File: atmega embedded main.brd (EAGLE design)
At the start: 354.1 x 155.8 mm, 144 parts, among them IC1 ATMEGA328PROUND, K100 SWITCH, K101 SWITCH, K102 SWITCH, K103 SWITCH, K104 SWITCH, K105 SWITCH, K106 SWITCH, K107 SWITCH, K108 SWITCH, K109 SWITCH, K110 SWITCH, K111 SWITCH, K112 SWITCH, K113 SWITCH, K114 SWITCH, K115 SWITCH, K116 SWITCH, K117 SWITCH, K118 SWITCH, K119 SWITCH, K120 SWITCH, K121 SWITCH, K122 SWITCH, K123 SWITCH, K124 SWITCH, K125 SWITCH, K126 SWITCH, K127 SWITCH, K128 SWITCH, K129 SWITCH, K130 SWITCH, K60 SWITCH, K67 SWITCH, K68 SWITCH, K69 SWITCH, K70 SWITCH, K71 SWITCH, K72 SWITCH, K73 SWITCH, K74 SWITCH, K75 SWITCH, K76 SWITCH, K77 SWITCH, K78 SWITCH, K79 SWITCH, K80 SWITCH, K81 SWITCH, K82 SWITCH, K83 SWITCH, K84 SWITCH, K85 SWITCH, K86 SWITCH, K87 SWITCH, K88 SWITCH, K89 SWITCH, K90 SWITCH, K91 SWITCH, K92 SWITCH, K93 SWITCH, K94 SWITCH, K95 SWITCH, K96 SWITCH, K97 SWITCH, K98 SWITCH, K99 SWITCH

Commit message: Flipped switches and rewired everything
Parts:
- moved R7 65.8 mm to (33.2, 114.0), turned to 90 degrees
- moved R6 64.6 mm to (35.6, 114.0), turned to 90 degrees
- moved D129 17.3 mm to (173.4, 4.75), flipped to the bottom, turned to 0 degrees
- moved D100 14.2 mm to (201.9, 80.8), flipped to the bottom
- moved D101 14.2 mm to (220.9, 80.8), flipped to the bottom
- moved D102 14.2 mm to (239.9, 80.8), flipped to the bottom
- moved D106 14.2 mm to (239.9, 61.8), flipped to the bottom
- moved D107 14.2 mm to (220.9, 61.8), flipped to the bottom
- moved D108 14.2 mm to (201.9, 61.8), flipped to the bottom
- moved D109 14.2 mm to (182.9, 61.8), flipped to the bottom
- moved D111 14.2 mm to (201.9, 4.75), flipped to the bottom
- moved D112 14.2 mm to (220.9, 4.75), flipped to the bottom
- moved D113 14.2 mm to (239.9, 4.75), flipped to the bottom
- moved D114 14.2 mm to (258.9, 4.75), flipped to the bottom
- moved D118 14.2 mm to (182.9, 42.8), flipped to the bottom
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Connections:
- new net N$42: D115.C, K104.P$1
- net COL1: now also IC1.11
- net COL10: now also IC1.3, K104.P$2; no longer K104.P$1
- net COL2: now also IC1.12
- net COL3: now also IC1.13
- net COL4: now also IC1.14
- net COL5: now also IC1.25
- net COL6: now also IC1.26, K118.P$2; no longer K118.P$1
- net COL7: now also IC1.27, K111.P$2, K128.P$2; no longer K111.P$1, K128.P$1
- net COL8: now also IC1.28, K105.P$2, K123.P$2; no longer K105.P$1, K123.P$1
- net COL9: now also IC1.2, K117.P$2, K98.P$2; no longer K117.P$1, K98.P$1
- net D+: now also R7.2; no longer IC1.23, R6.1, R6.2
- net D-: now also R6.2; no longer R7.2
- net N$21: now also IC1.6; no longer IC1.24
- net N$27: now also D116.C, K98.P$1; no longer D98.C, K118.P$2
- net N$28: now also D117.C, K105.P$1; no longer D110.C, K111.P$2
- net N$40: now also D110.C, K111.P$1; no longer D117.C, K105.P$2
- net N$41: now also D98.C, K118.P$1; no longer D116.C, K98.P$2
- net N$65: now also D128.C, K117.P$1; no longer D115.C, K104.P$2
- net N$66: now also D127.C, K123.P$1; no longer D128.C, K117.P$2
- net N$67: now also D104.C, K128.P$1; no longer D127.C, K123.P$2
- net N$68: now also IC1.5, R6.1; no longer D104.C, K128.P$2
- net ROW1: now also IC1.23
- net ROW2: now also IC1.19
- net ROW3: now also IC1.18
- net ROW4: now also IC1.17
- net ROW5: now also IC1.16
- net ROW6: now also IC1.15
- net ROW7: now also IC1.24
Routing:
- net COL9: track 109.5 -> 436.6 mm, vias 0 -> 2
- net COL8: track 104.0 -> 408.8 mm, vias 0 -> 2
- net ROW6: track 170.5 -> 462.1 mm, vias 0 -> 2
- net COL7: track 104.0 -> 393.0 mm, vias 0 -> 2
- net ROW3: track 369.7 -> 645.3 mm, vias 0 -> 2
- net ROW5: track 479.1 -> 751.6 mm, vias 0 -> 2
- net ROW4: track 389.8 -> 659.2 mm, vias 0 -> 2
- net ROW2: track 330.0 -> 599.1 mm, vias 0 -> 2
- net COL10: track 110.5 -> 351.7 mm, vias 0 -> 2
- net COL4: track 104.0 -> 329.2 mm, vias 0 -> 1
- net COL3: track 104.0 -> 326.7 mm, vias 0 -> 1
- net COL2: track 116.6 -> 321.6 mm, vias 0 -> 1
- net COL5: track 111.2 -> 303.2 mm, vias 0 -> 1
- net COL6: track 104.4 -> 287.2 mm, vias 0 -> 2
- net ROW7: track 119.7 -> 270.6 mm, vias 0 -> 2
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
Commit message: Compacted stuff around the chip
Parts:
- moved C3 29.0 mm to (106.9, 106.9)
- moved R5 28.2 mm to (78.4, 104.5)
- moved C4 27.1 mm to (102.1, 106.9)
- moved S1 26.6 mm to (83.1, 97.4)
- moved C5 25.2 mm to (97.4, 106.9)
- moved C6 23.5 mm to (92.6, 106.9)
- moved C7 21.9 mm to (87.9, 106.9)
- moved C10 18.6 mm to (37.4, 114.0), turned to 0 degrees
- moved U1 18.1 mm to (73.6, 115.2)
- moved C9 16.4 mm to (37.4, 111.6), turned to 0 degrees
- moved R7 12.2 mm to (44.5, 109.2), flipped to the bottom
- moved Q1 9.67 mm to (30.9, 112.2), turned to 313.5 degrees
- moved IC1 8.56 mm to (35.6, 102.1)
- moved R6 7.60 mm to (41.6, 109.2)
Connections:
- net N$21: now also IC1.4; no longer IC1.6
- net ROW5: now also IC1.15; no longer IC1.16
- net ROW6: now also IC1.16; no longer IC1.15
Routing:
- net GND: track 80.6 -> 148.2 mm, vias 4 -> 3
- net VCC: track 51.2 -> 114.8 mm
- net ROW5: track 751.6 -> 770.8 mm
- net N$15: track 17.7 -> 36.2 mm
- net ROW6: track 462.1 -> 475.9 mm
- net COL10: track 351.7 -> 340.8 mm
- net ROW7: track 270.6 -> 260.1 mm
- net COL4: track 329.2 -> 319.3 mm
- net COL6: track 287.2 -> 277.7 mm
- net COL3: track 326.7 -> 317.6 mm
- net ROW1: track 376.0 -> 383.8 mm
- net COL9: track 436.6 -> 428.9 mm
- net D-: track 39.3 -> 46.8 mm
- net COL8: track 408.8 -> 401.5 mm
- net COL1: track 212.0 -> 204.9 mm
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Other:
- board size 354.1 x 155.8 mm -> 313.5 x 125.9 mm

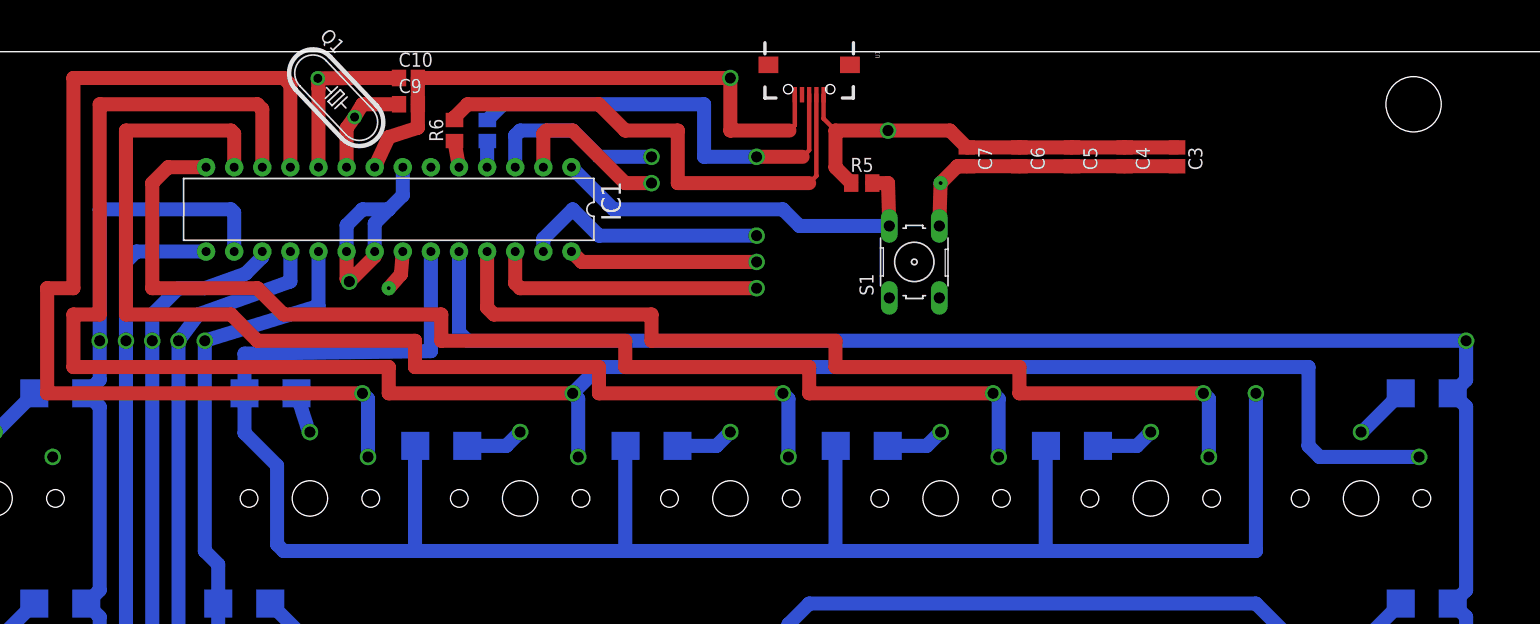
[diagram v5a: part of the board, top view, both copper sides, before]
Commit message: Fixed errors and made adjustments for USB
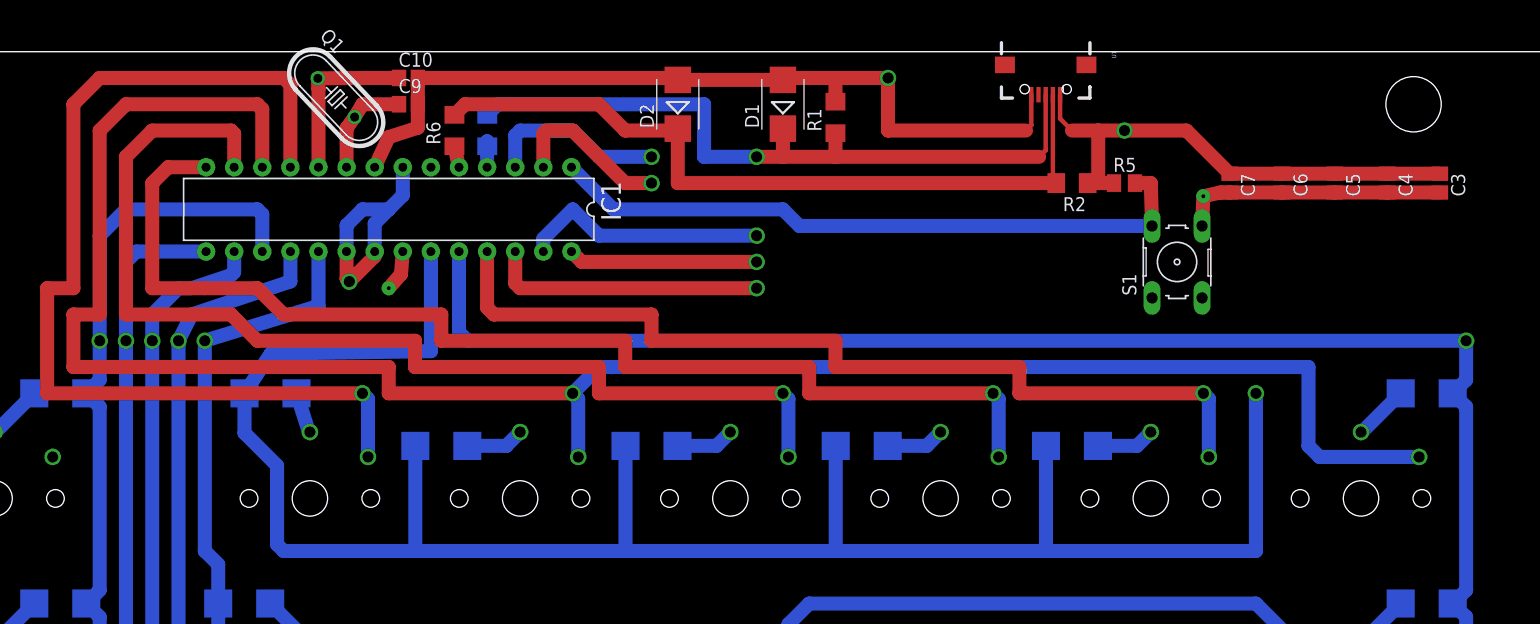
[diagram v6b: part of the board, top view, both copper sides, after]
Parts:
- added D1, D2: 3.6, diode:SMB
- added R1: 1M, eagle-ltspice:R1206
- added R2: 1.5K, eagle-ltspice:R1206
- R6, R7: value 22 -> 68; device adafruit:M0805 -> eagle-ltspice:R1206
- moved C3 23.9 mm to (130.6, 104.5)
- moved C4 23.9 mm to (125.9, 104.5)
- moved C5 23.9 mm to (121.1, 104.5)
- moved C6 23.9 mm to (116.4, 104.5)
- moved C7 23.9 mm to (111.6, 104.5)
- moved R5 23.8 mm to (102.1, 104.5)
- moved S1 23.8 mm to (106.9, 97.4)
- moved U1 21.4 mm to (95.0, 115.2)
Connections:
- net D+: now also D1.C, R1.1
- net D-: now also D2.C, R2.2
- net GND: now also D1.A, D2.A, R1.2
- net ROW4: now also IC1.16; no longer IC1.17
- net ROW6: now also IC1.17; no longer IC1.16
- net VCC: now also R2.1
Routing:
- net GND: track 148.2 -> 185.5 mm
- net D+: track 39.7 -> 65.6 mm
- net VCC: track 114.8 -> 139.8 mm
- net N$15: track 36.2 -> 60.0 mm
- net D-: track 46.8 -> 68.9 mm
- net ROW4: track 659.9 -> 658.2 mm
- net ROW1: track 383.8 -> 382.2 mm
- net COL3: track 317.6 -> 316.3 mm
- net COL2: track 315.8 -> 314.4 mm
- net COL1: track 204.9 -> 203.5 mm
- net ROW6: track 475.9 -> 477.0 mm
- net ROW5: track 770.8 -> 771.5 mm
- net COL7: track 385.9 -> 386.5 mm
